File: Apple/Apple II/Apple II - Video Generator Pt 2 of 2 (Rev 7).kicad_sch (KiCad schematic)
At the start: 0 parts

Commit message: Finished Apple II - Sheet 19 - Video Generator Part 2 (Rev 7)
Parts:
- added A14: 74LS02, symbol Apple II:A14_74LS02
- added A?: 74LS02, symbol Apple II:A12_74LS02
- added B? (x4): 74LS02, symbol Apple II:B14_74LS02
- added B?: 74LS11, symbol Apple II:B12_74LS11
- added B?: 74LS02, symbol Apple II:B13_74LS02
- added B?: 74LS08, symbol Apple II:B11_74LS08
- added C2: 47pF, symbol Device:C_Small
- added C3: 5-50pF, symbol Device:C_Variable
- added C?: 74LS32, symbol Apple II:C14_74LS32
- added C?: 74LS04, symbol Apple II:C11_74LS04
- added J?: AUX VIDEO PIN, symbol Connector:Conn_01x04_Male
- added J?: COMPOSITE VIDEO OUTPUT, symbol Connector:Conn_Coaxial
- added J?: AUX VIDEO CONNECTOR, symbol Connector:Conn_01x04_Male
- added JP?: 13, symbol Jumper:SolderJumper_2_Open
- added JP?: 16, symbol Apple II:Bowtie_SolderJumper
- added JP?: 14, symbol Jumper:SolderJumper_2_Open
- added JP?: 12, symbol Apple II:Bowtie_SolderJumper
- added L1: 27µH, symbol Device:L
- added N1: 1, symbol Apple II:NOTE_NUMBER
- added N2: 2, symbol Apple II:NOTE_NUMBER
- added Q3, Q6, Q7: 2N3904, Package_TO_SOT_THT:TO-92_Inline, symbol Transistor_BJT:2N3904
- added R10: 27Ω, symbol Device:R_US
- added R11: 200Ω, symbol Device:R_Potentiometer_US
- added R27: 4.7K, symbol Device:R_US
- added R33, R34, R8: 2K, symbol Device:R_US
- added R35, R7: 1.5K, symbol Device:R_US
- added R5: 1K, symbol Device:R_US
- added R6: 2.7K, symbol Device:R_US
- added R9: 10Ω, symbol Device:R_US
- added TP? (x3): TestPoint, symbol Connector:TestPoint
- added U? (x2): C13_74LS51, symbol Apple II:C13_74LS51
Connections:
- new net: J?.2 (Pin_2), Q3.1 (E), R11.1
- new net: J?.1 (Pin_1), R10.1, R11.2
- new net: Q6.2 (B), R27.2
- new net: B?.2, JP?.2 (B), JP?.2 (B)
- new net: C2.1, C3.1, L1.1, Q6.3 (C), R5.2, R6.1
- new net: Q3.2 (B), R6.2, R7.2, R8.2
- new net: Q3.3 (C), R9.1
- new net: B?.3, B?.4
- new net: Q7.2 (B), R33.2, R34.2
- new net: A14.1, A14.5
- new net: A14.2, A14.3
- new net: B?.11, JP?.2 (B), JP?.2 (B)
- new net: B?.1, B?.1
- new net: J?.4 (Pin_4), TP?.1
- new net: J?.3 (Pin_3), TP?.1
- new net: A?.4, B?.12
- new net: A?.5, A?.6, B?.10
- new net: B?.1, U?.1
- new net: B?.3, Q7.3 (C), R35.1, U?.10
- new net: J?.1 (In), R10.2
- new net: C?.10, JP?.1 (A)
- new net: B?.13, U?.12
- new net: B?.8, C?.4, U?.13
- new net +12V: J?.4 (Pin_4)
- new net +5V: R35.2, R9.2
- new net -5V: J?.3 (Pin_3)
- new net AN2: J?.2 (Pin_2), TP?.1
- new net BLANKING: C?.6
- new net COLOR_BURST: B?.12, R5.1
- new net COLOR_REF_{35}: B?.2
- new net Earth: C2.2, C3.2, J?.1 (Pin_1), J?.2 (Ext), L1.2, Q6.1 (E), Q7.1 (E), R11.3, R33.1
- new net H2: R34.1
- new net H3: B?.2, U?.11, U?.3
- new net H4: B?.5, U?.2
- new net H5: B?.6, U?.4, U?.5
- new net HBL: B?.13, C?.5, U?.6, U?.9
- new net SYNC_{19}: R8.1, U?.8
- new net TEXT MODE: R27.1
- new net V0: B?.9
- new net V1: JP?.1 (A)
- new net V2: C?.11, JP?.1 (A)
- new net V3: B?.9
- new net V4: B?.10
- new net V5: JP?.1 (A)
- new net VC: B?.8
- new net VIDEO_DATA: R7.1
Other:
- note added: "FROM CLOCK GENERATOR"
- note added: "FROM ON-BOARD I/O"
- note added: "FROM ON-BOARD I/O PT1"
- note added: "FROM PART 1"
- note added: "FROM VIDEO ADDRESS GENERATOR"
- note added: "TO MEMORY ADDRESS PT 1"
- note added: "TO PART 1"
- note added: "TO PERIPHREAL I/O"
- title: (none) -> Apple II - Video Generator Part 2

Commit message: End of day cleanup
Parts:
- added N1: 1, symbol Apple II:NOTE_NUMBER
- added N2: 2, symbol Apple II:NOTE_NUMBER
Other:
- note added: "4-PIN CONNECTOR ON SOME REV.7 BOARDS"
- note added: "ADDITIONAL COLOR KILLER CIRCUIT ON LATER REV. 7 BOARDS"
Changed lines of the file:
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@@
     (stroke (width 0) (type default) (color 0 0 0 0))
+  )
+  (text "4-PIN CONNECTOR ON SOME REV.7 BOARDS" (at 303.53 250.19 0)
+    (effects (font (size 1.27 1.27)) (justify left bottom))
   )
   (text "FROM\nON-BOARD I/O" (at 41.402 45.974 180)
@@
   (text "TO\nPERIPHREAL I/O" (at 335.788 193.294 0)
     (effects (font (size 0.96 0.96)) (justify left bottom))
+  )
+  (text "ADDITIONAL COLOR KILLER CIRCUIT ON LATER\nREV. 7 BOARDS"
+    (at 303.53 245.11 0)
+    (effects (font (size 1.27 1.27)) (justify left bottom))
   )
   (text "FROM CLOCK\nGENERATOR" (at 38.862 56.134 180)
@@
     (pin "13")
   )
+  (symbol (lib_id "Apple II:NOTE_NUMBER") (at 300.99 248.92 0) (unit 1)
+    (in_bom yes) (on_board yes)
+    (property "Reference" "N2" (id 0) (at 293.37 243.84 0)
+      (effects (font (size 1.27 1.27)) hide)
+    )
+    (property "Value" "2" (id 1) (at 300.99 248.92 0))
+    (property "Footprint" "" (id 2) (at 300.99 248.92 0)
+      (effects (font (size 1.27 1.27)) hide)
+    )
+    (property "Datasheet" "" (id 3) (at 300.99 248.92 0)
+      (effects (font (size 1.27 1.27)) hide)
+    )
+  )
   (symbol (lib_id "Apple II:NOTE_NUMBER") (at 137.16 26.67 0) (unit 1)
     (in_bom yes) (on_board yes)
@@
     (pin "13")
   )
+  (symbol (lib_id "Apple II:NOTE_NUMBER") (at 300.99 242.57 0) (unit 1)
+    (in_bom yes) (on_board yes)
+    (property "Reference" "N1" (id 0) (at 293.37 237.49 0)
+      (effects (font (size 1.27 1.27)) hide)
+    )
+    (property "Value" "1" (id 1) (at 300.99 242.57 0))
+    (property "Footprint" "" (id 2) (at 300.99 242.57 0)
+      (effects (font (size 1.27 1.27)) hide)
+    )
+    (property "Datasheet" "" (id 3) (at 300.99 242.57 0)
+      (effects (font (size 1.27 1.27)) hide)
+    )
+  )
   (symbol (lib_id "Device:R_US") (at 300.99 152.4 90) (unit 1)

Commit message: Finished Apple II - Sheet 20 - Video Generator Part 2 (Rev RFI)
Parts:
- added C13, C14: 0.1µF, symbol Device:C_Small
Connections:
- net +12V: now also C14.1
- net -5V: now also C13.1
- net Earth: now also C13.2, C14.2

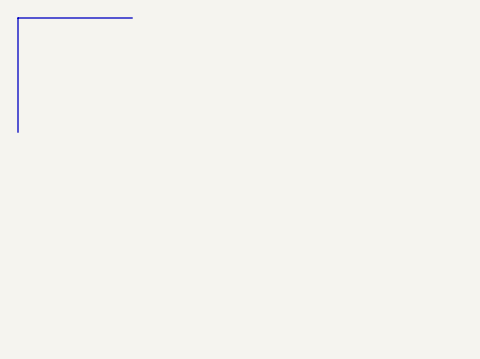
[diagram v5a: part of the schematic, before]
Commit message: Finished Apple II - Sheet 22 - Two-Piece Keyboard
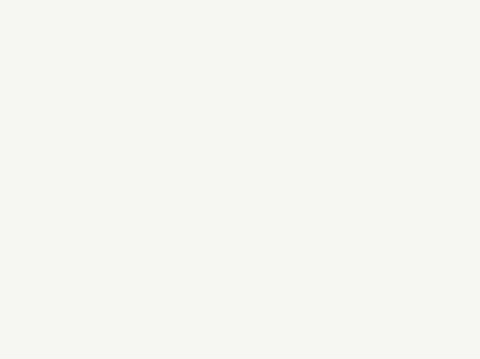
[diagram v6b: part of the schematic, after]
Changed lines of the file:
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@@
-    (stroke (width 0) (type default) (color 0 0 0 0))
-  )
-  (polyline (pts (xy 0 0) (xy 0 12.7))
     (stroke (width 0) (type default) (color 0 0 0 0))
   )
@@
     (stroke (width 0) (type default) (color 0 0 0 0))
   )
-  (polyline (pts (xy 12.7 0) (xy 0 0))
-    (stroke (width 0) (type default) (color 0 0 0 0))
-  )
